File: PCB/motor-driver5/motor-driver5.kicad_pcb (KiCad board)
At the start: 2 copper layers, 72 x 50 mm, 54 parts, among them J1 Motor Power, J2 Logic Power, J3 Input Ch1, J4 Input Ch2, M1 Motor_DC, M2 Motor_DC, Q1 Q_PMOS_GDS, Q2 Q_NMOS_GDS, Q3 Q_PMOS_GDS, Q4 Q_NMOS_GDS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

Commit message: 完成
git-svn-id: https://shiro-home.ddns.net/svn/project/motor-driver/trunk@15 73406841-da20-4056-b287-c5b29fcc9b8e
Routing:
- net GNDPWR: vias 20 -> 24

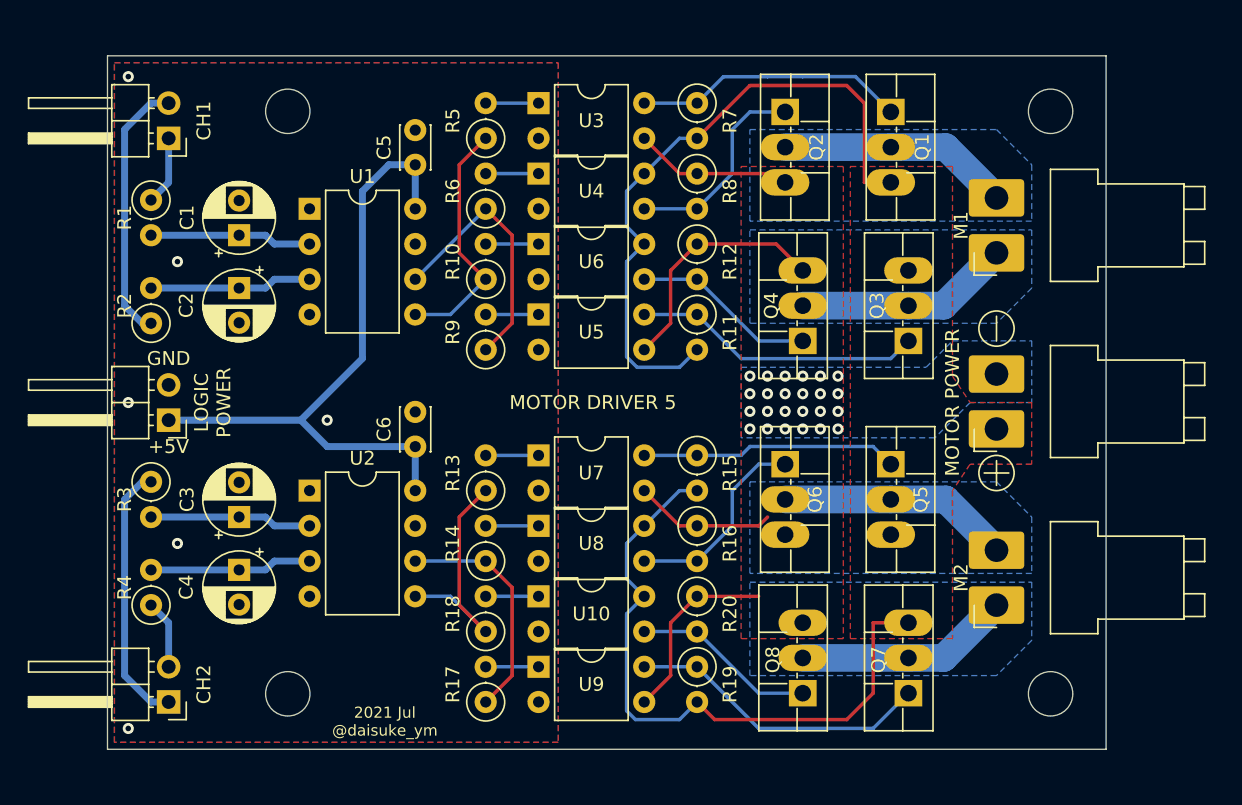
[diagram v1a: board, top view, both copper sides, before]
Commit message: 電源ラインが細かったので，基板サイズを大きくして太く修正した。
git-svn-id: https://shiro-home.ddns.net/svn/project/motor-driver/trunk@19 73406841-da20-4056-b287-c5b29fcc9b8e
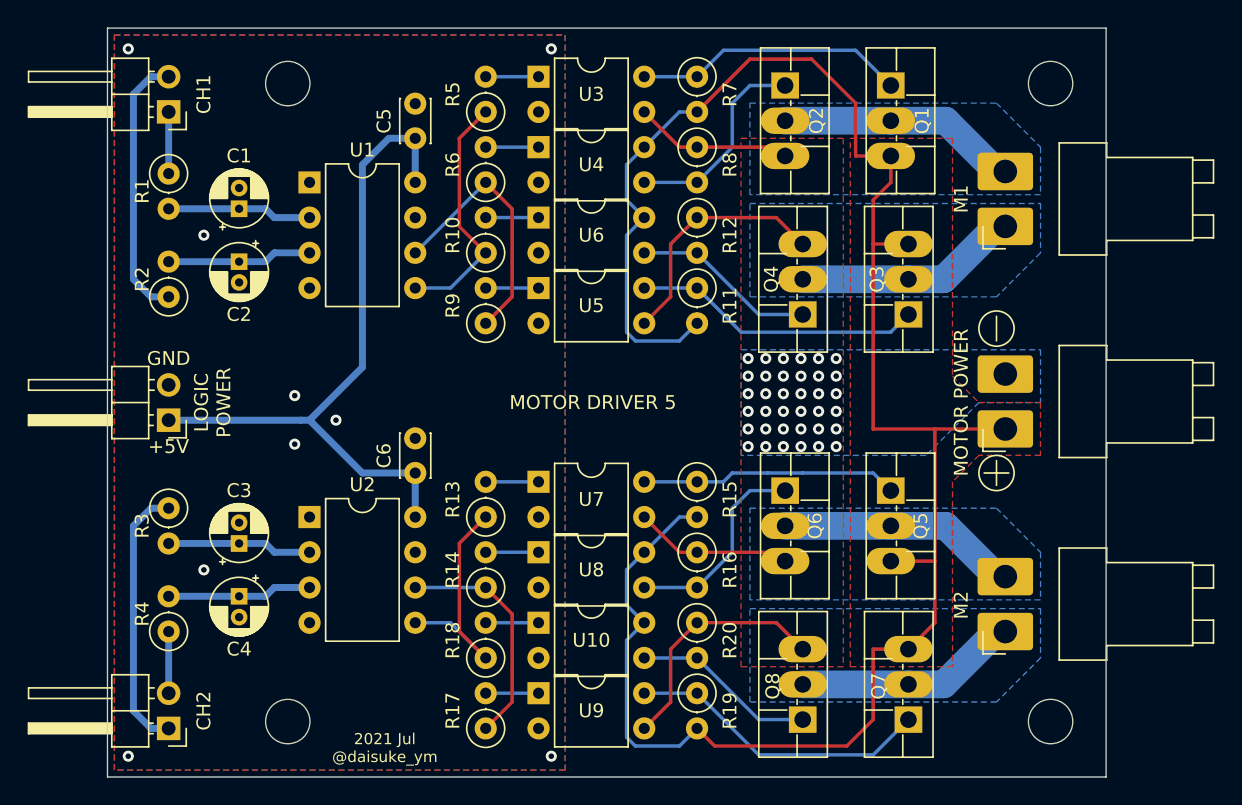
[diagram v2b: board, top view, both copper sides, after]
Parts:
- C1, C2, C3, C4: footprint Capacitor_THT:CP_Radial_D5.0mm_P2.50mm -> Capacitor_THT:CP_Radial_D4.0mm_P1.50mm
- moved R1 2.29 mm to (128.4, 83.5)
- moved R2 2.29 mm to (128.4, 92.4)
- moved R3 2.29 mm to (128.4, 107.6)
- moved R4 2.29 mm to (128.4, 116.5)
- moved M1 2.01 mm to (188.7, 87.3)
- moved M2 2.01 mm to (188.7, 116.5)
- moved REF** 2.00 mm to (192.0, 77.0)
- moved REF** 2.00 mm to (192.0, 123.0)
- moved REF** 2.00 mm to (137.0, 123.0)
- moved REF** 2.00 mm to (137.0, 77.0)
- moved C1 1.91 mm to (133.5, 86.0)
- moved C2 1.91 mm to (133.5, 89.8)
- moved C3 1.91 mm to (133.5, 110.2)
- moved C4 1.91 mm to (133.5, 114.0)
- moved C5 1.91 mm to (146.2, 81.0)
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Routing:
- net +BATT: track 94.6 -> 145.7 mm
- net GNDPWR: track 52.9 -> 58.2 mm, vias 24 -> 36
- net +5V: track 48.0 -> 50.4 mm
- net /IN2AA: track 11.8 -> 10.5 mm
- net /IN1BA: track 11.7 -> 10.4 mm
- net /IN2BA: track 11.7 -> 10.4 mm
- net /IN1AA: track 11.7 -> 10.4 mm
- net /IN2B: track 4.97 -> 4.44 mm
- net /IN1A: track 4.97 -> 4.44 mm
- net GND: vias 6 -> 9
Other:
- board size 72 x 50 mm -> 72 x 54 mm
